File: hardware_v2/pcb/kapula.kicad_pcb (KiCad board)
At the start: 4 copper layers, 50 x 59 mm, 167 parts, among them J1 Conn_02x10_Odd_Even, J2 Conn_02x10_Odd_Even, J3 U.FL, J4 U.FL, J5 U.FL, J6 U.FL, Q1 AO3401A, Q2 AO3400A, Q3 AO3400A, Q4 AO3400A, Q5 AO3401A, Q6 BSS84, T1 BW21S7511A01TF, T2 BW21S7511A01TF, T3 BW21S7511A01TF, T4 BW21S7511A01TF, U1 TP4054, U2 DW01+G, U3 XC6206P332MR, U4 FM8002A, U5 EFR32FG14P233F256GM48-B, U6 TG2016SMN 38.4000M-MCGNNM3, U7 XA213-G4J, Y1 32768 Hz

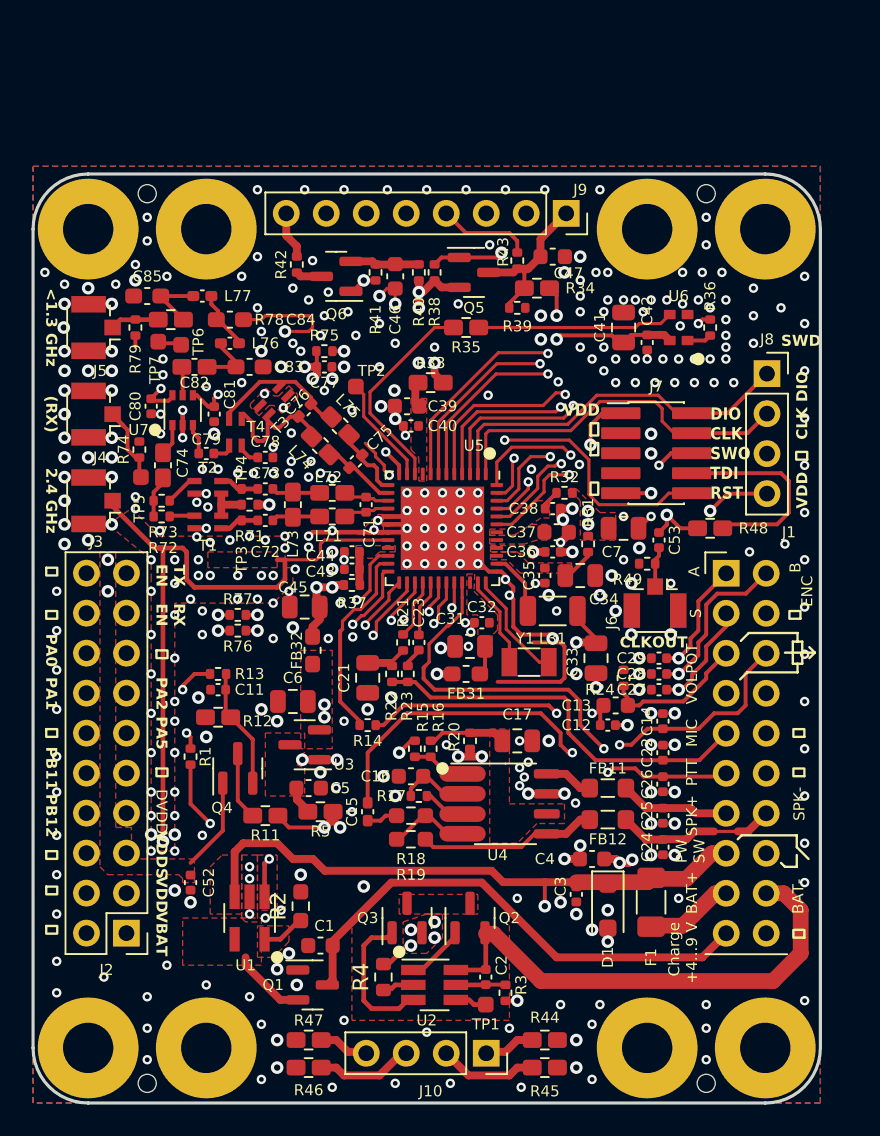
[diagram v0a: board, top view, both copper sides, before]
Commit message: PCB: Change some resistor footprints and package sizes
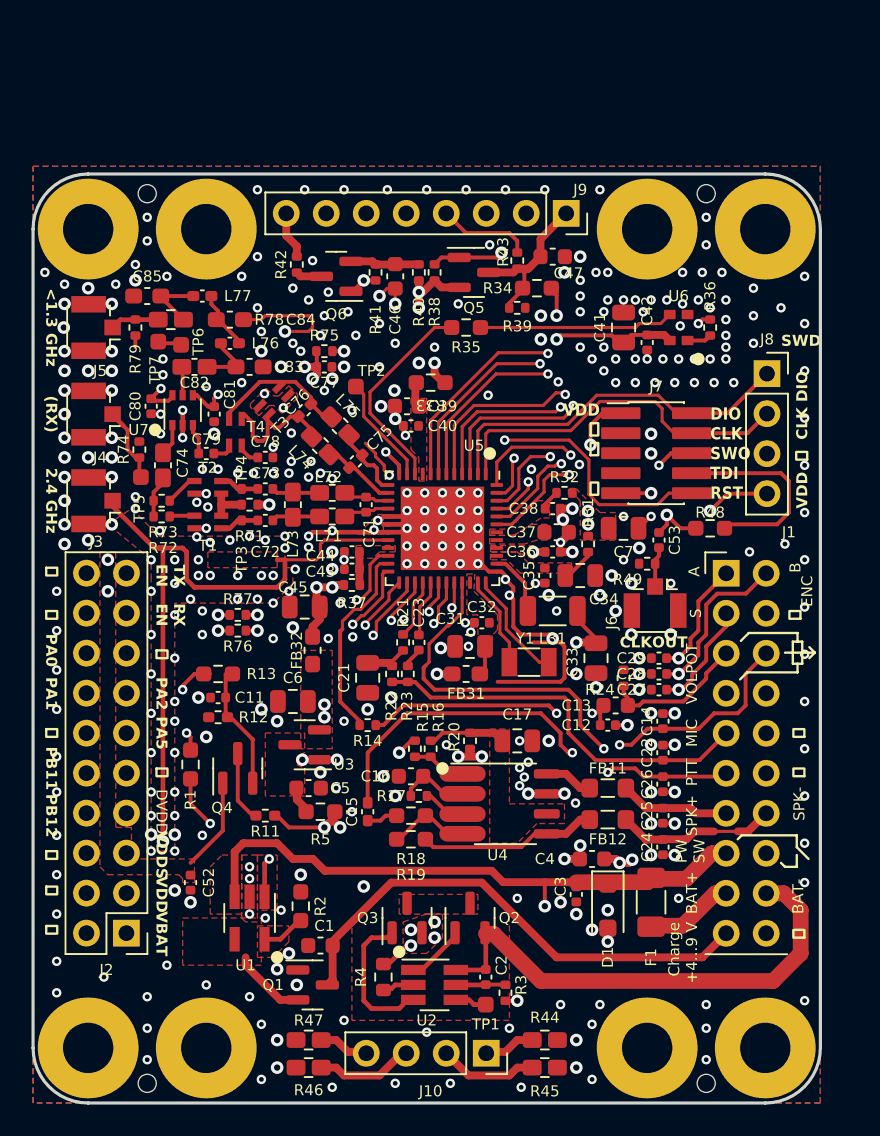
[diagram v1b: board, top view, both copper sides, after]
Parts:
- R1, R13: footprint Resistor_SMD:R_0402_1005Metric -> Resistor_SMD:R_0603_1608Metric_Pad0.98x0.95mm_HandSolder
- R11, R12: footprint kapula:R_0402_to_0603_HandSolder -> Resistor_SMD:R_0402_1005Metric_Pad0.72x0.64mm_HandSolder
- R33, R34, R35, R48, R5: footprint kapula:R_0402_to_0603_HandSolder -> Resistor_SMD:R_0603_1608Metric_Pad0.98x0.95mm_HandSolder
- moved C11 0.50 mm to (111.8, 90.8)
- moved R1 0.50 mm to (110.0, 95.0)
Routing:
- net /~{CHRG}: track 11.5 -> 10.6 mm

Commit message: PCB: Change version number in silkscreen
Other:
- board text added: "Gekkokapula v2.2"
- board text added: "OH2EAT 2024"
- board text removed: "Gekkokapula v2.1"
- board text removed: "OH2EAT 2023"
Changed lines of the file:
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@@
     (effects (font (size 0.7 0.7) (thickness 0.15)) (justify bottom mirror))
   )
-  (gr_text "Gekkokapula v2.1" (at 125 67.75) (layer "B.SilkS")
+  (gr_text "Gekkokapula v2.2" (at 125 67.75) (layer "B.SilkS")
     (effects (font (size 1.5 1.5) (thickness 0.3) bold) (justify mirror))
   )
@@
     (effects (font (size 0.7 0.7) (thickness 0.15)) (justify top mirror))
   )
-  (gr_text "OH2EAT 2023" (at 125 70.25) (layer "B.SilkS")
+  (gr_text "OH2EAT 2024" (at 125 70.25) (layer "B.SilkS")
     (effects (font (size 0.7 0.7) (thickness 0.15) bold) (justify mirror))
   )

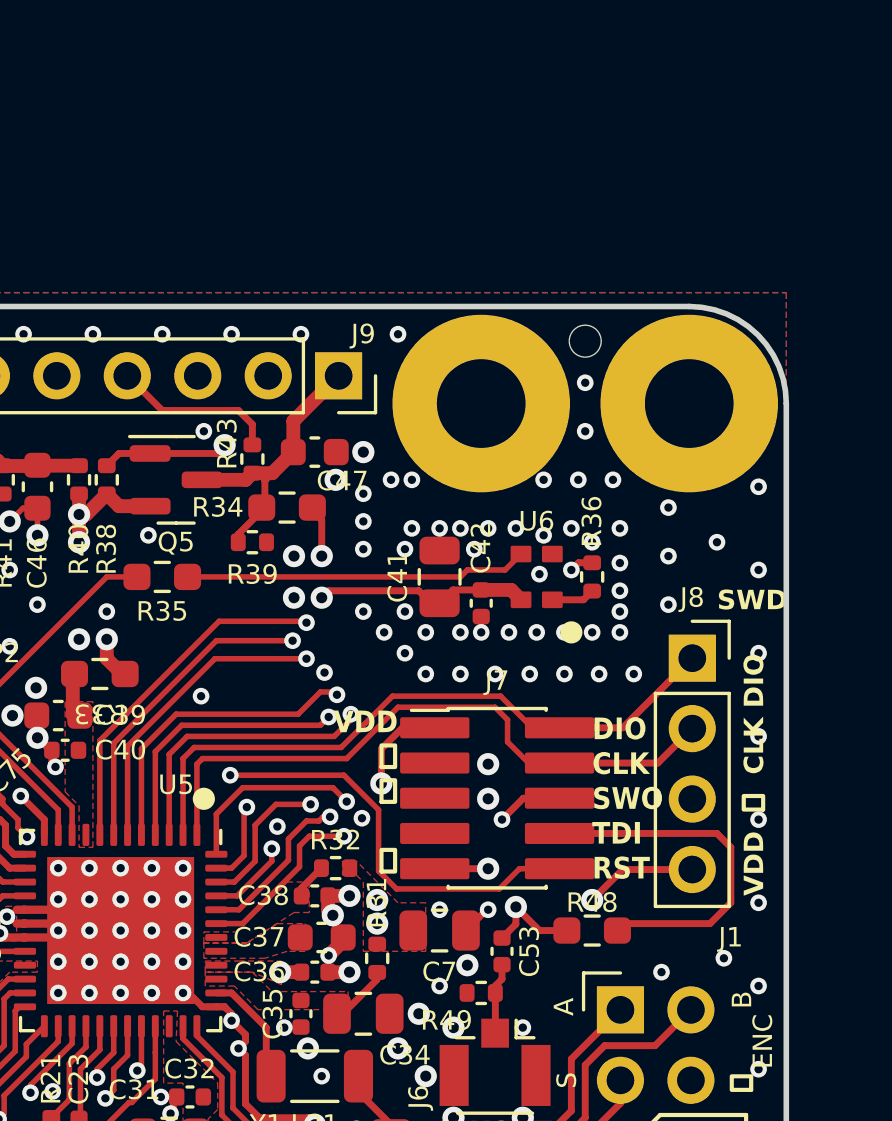
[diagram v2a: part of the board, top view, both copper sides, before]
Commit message: PCB: Change SWD/JTAG connector to 2.54 mm pitch
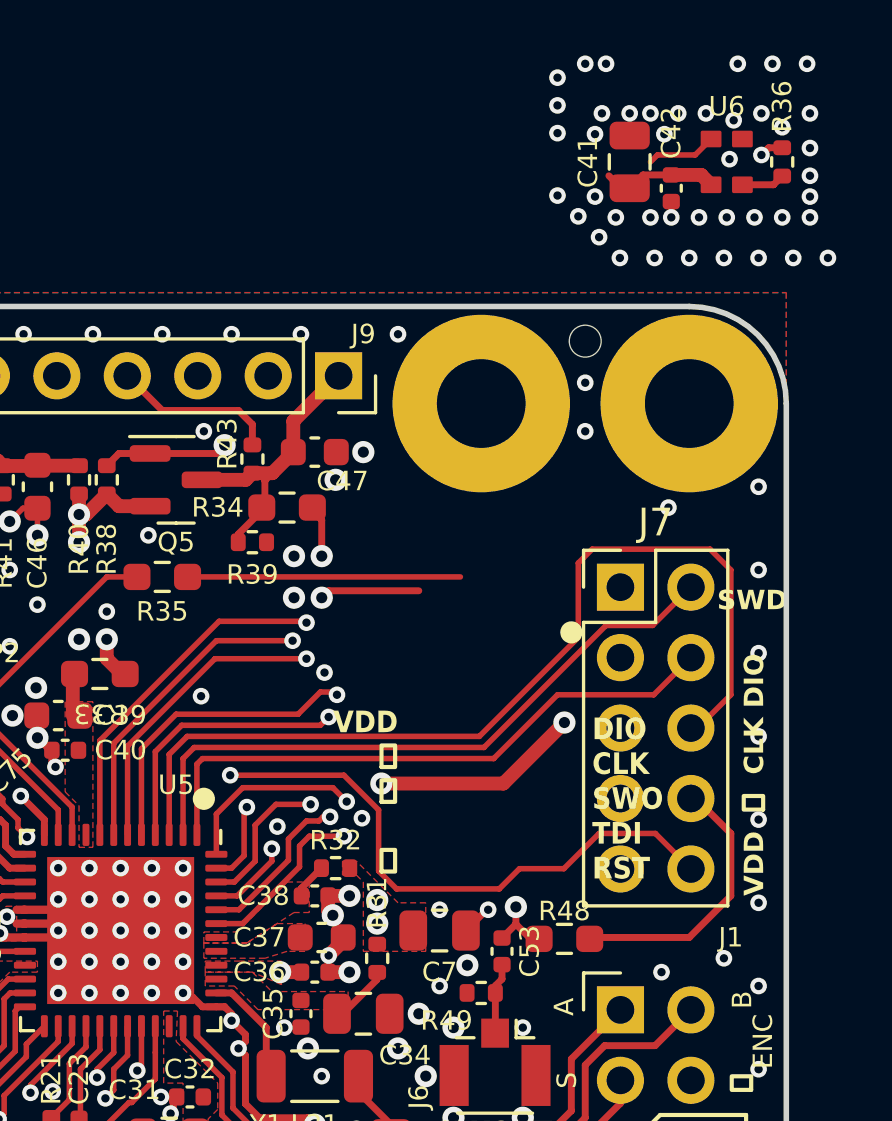
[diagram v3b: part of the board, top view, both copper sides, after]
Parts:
- removed J8: ~, Connector_PinSocket_2.54mm:PinSocket_1x04_P2.54mm_Vertical
- J7: footprint kapula:DZ127S-22-10-55 -> Connector_PinHeader_2.54mm:PinHeader_2x05_P2.54mm_Vertical
- moved C42 16.5 mm to (145.9, 53.2)
- moved C41 16.5 mm to (144.4, 52.3)
- moved R36 16.5 mm to (149.9, 52.3)
- moved U6 16.5 mm to (147.9, 52.3)
- moved J7 8.81 mm to (144.0, 67.6)
- moved R48 1.04 mm to (142.0, 80.3)
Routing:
- net /SWO_TDO: track 19.3 -> 34.5 mm, vias 2 -> 0
- net /Knob_S: track 54.7 -> 47.6 mm
- net /Knob_B: track 54.9 -> 47.9 mm
- net /SPK_SDN: track 60.6 -> 53.6 mm
- net /Knob_A: track 48.9 -> 42.0 mm
- net /RESET: track 44.2 -> 49.9 mm
- net Net-(J7-NC/TDI): track 13.4 -> 9.94 mm
- net /VDD: track 22.2 -> 19.0 mm
- net /PF3_TDI: track 24.2 -> 22.3 mm
- net GND: track 64.7 -> 63.0 mm, vias 394 -> 388
- net /SWCLK_TCK: track 23.1 -> 22.0 mm

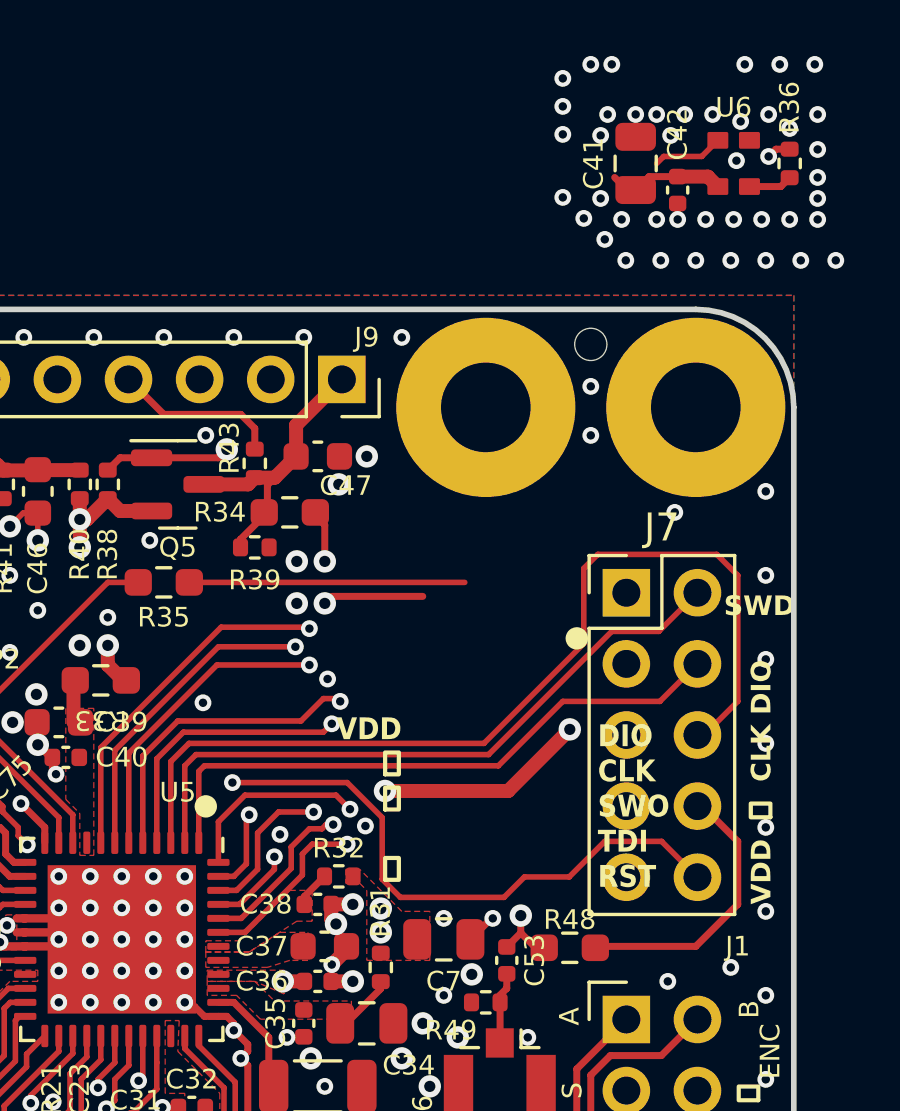
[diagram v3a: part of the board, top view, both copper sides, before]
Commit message: PCB: Make some space for TCXO again
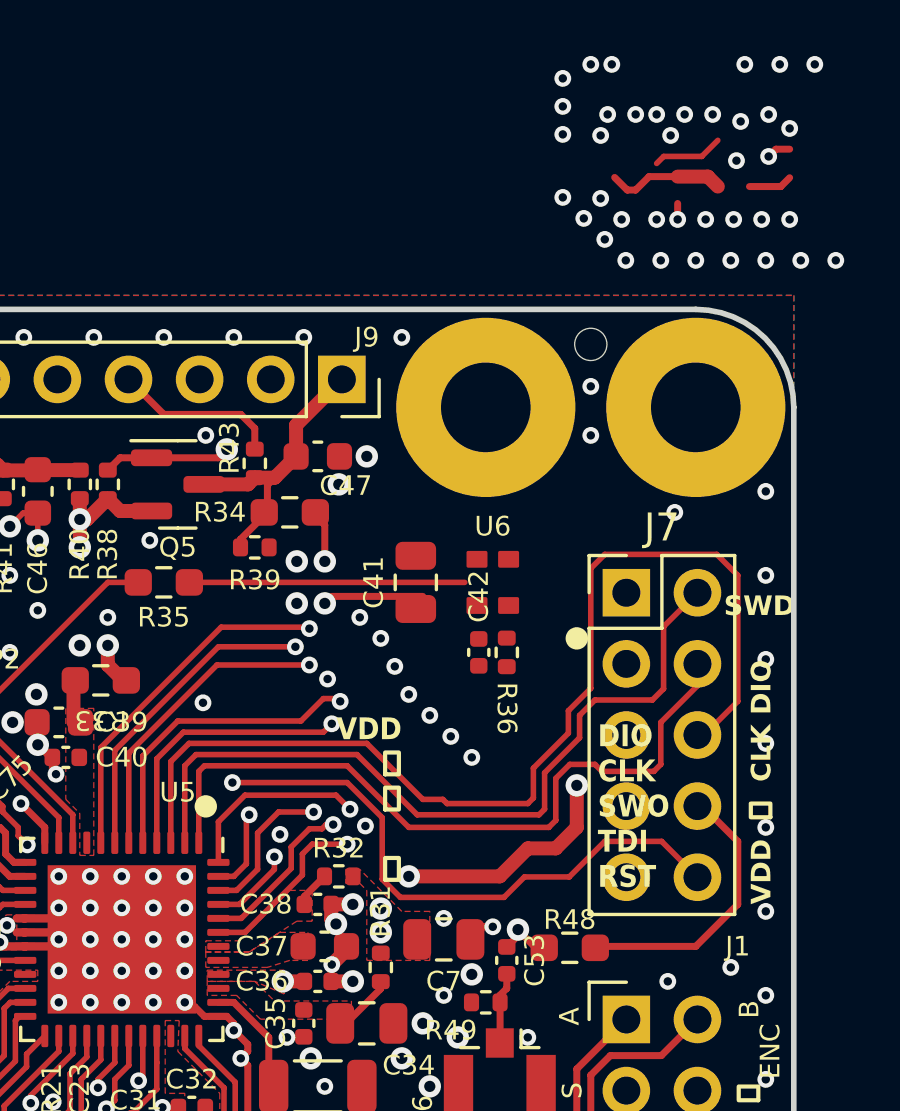
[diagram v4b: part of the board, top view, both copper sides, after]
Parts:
- moved R36 20.2 mm to (139.8, 69.8), turned to -90 degrees
- moved C42 18.0 mm to (138.8, 69.8)
- moved U6 17.3 mm to (139.2, 67.2)
- moved C41 16.9 mm to (136.5, 67.2)
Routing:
- net /SWDIO_TMS: track 23.6 -> 27.9 mm
- net /SWCLK_TCK: track 22.0 -> 26.2 mm
- net /SWO_TDO: track 34.5 -> 38.3 mm
- net /VDD: track 19.0 -> 21.6 mm
- net GND: track 63.0 -> 62.9 mm, vias 388 -> 390

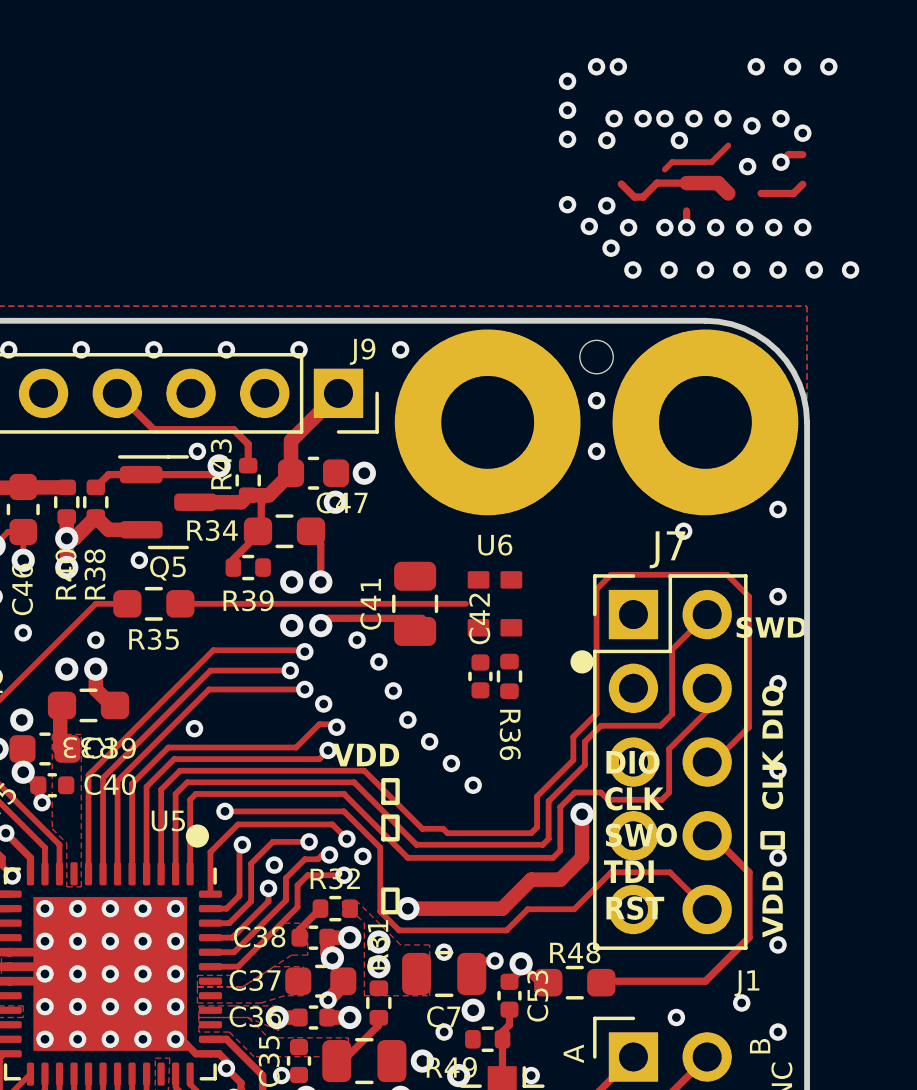
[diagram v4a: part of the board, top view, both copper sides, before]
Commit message: PCB: Route TCXO again
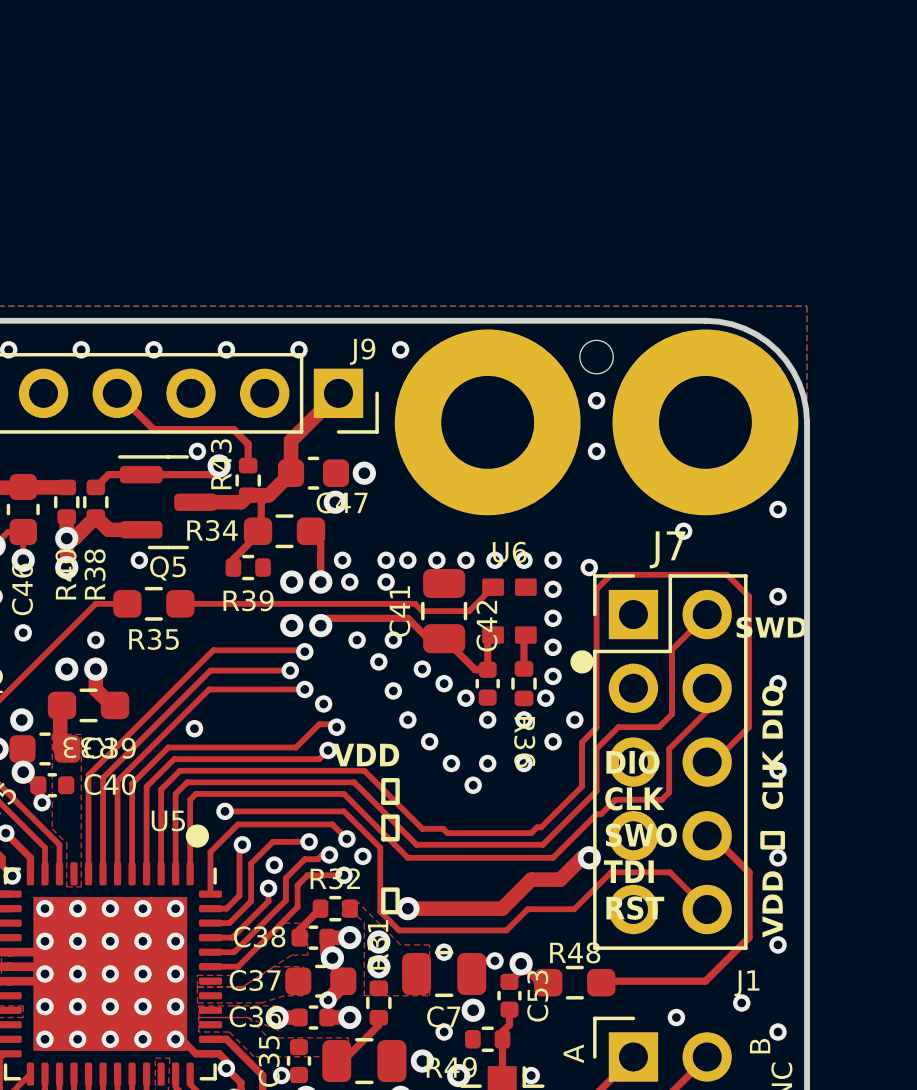
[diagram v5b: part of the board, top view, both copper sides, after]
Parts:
- moved C41 1.03 mm to (137.5, 67.5)
- moved R36 0.56 mm to (140.2, 70.0)
- moved U6 0.56 mm to (139.8, 67.5)
- moved C42 0.35 mm to (139.0, 70.0)
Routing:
- net /VDD: track 21.6 -> 12.7 mm
- net GND: track 62.9 -> 61.5 mm, vias 390 -> 378
- net /TCXOout: track 12.5 -> 11.3 mm
- net /SWCLK_TCK: track 26.2 -> 25.1 mm
